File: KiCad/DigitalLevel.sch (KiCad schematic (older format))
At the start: 4 parts

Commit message: Adding KiCad PDF
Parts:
- removed U?: LD1117S33TR_SOT223, Package_TO_SOT_SMD:SOT-223-3_TabPin2, symbol Regulator_Linear:LD1117S33TR_SOT223
- added C1: 2200p, symbol Device:C
- added C2: 0.1u, symbol Device:C
- added C3: 0.01u, symbol Device:C
- added C4: 10n, symbol Device:C
- added R1, R2: 10k, symbol Device:R
- added U2: MPU-6050, Sensor_Motion:InvenSense_QFN-24_4x4mm_P0.5mm, symbol Sensor_Motion:MPU-6050
- added U3: XC6206P332MR, Package_TO_SOT_SMD:SOT-23, symbol Regulator_Linear:XC6206PxxxMR
- C5, C6: renamed from C?; value C -> 1u
- gave numbers to parts that had none: 1
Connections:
- net labels added: INT, SCL, SDA, VCC, VIN, VOUT, XCL, XDA
- wire segments 14 -> 55
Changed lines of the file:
@@
 $EndDescr
 $Comp
-L MCU_ST_STM32F1:STM32F103R6Tx U?
+L MCU_ST_STM32F1:STM32F103R6Tx U1
 U 1 1 5E2E5CE7
 P 3900 3550
-F 0 "U?" H 3900 1661 50  0000 C CNN
+F 0 "U1" H 3900 1661 50  0000 C CNN
 F 1 "STM32F103R6Tx" H 3900 1570 50  0000 C CNN
 F 2 "Package_QFP:LQFP-64_10x10mm_P0.5mm" H 3300 1850 50  0001 R CNN
 F 3 "http://www.st.com/st-web-ui/static/active/en/resource/technical/document/datasheet/CD00210843.pdf" H 3900 3550 50  0001 C CNN
 	1    3900 3550
-	1    0    0    -1
-$EndComp
-$Comp
-L Regulator_Linear:LD1117S33TR_SOT223 U?
-U 1 1 5E308040
-P 8200 2700
-F 0 "U?" H 8200 2942 50  0000 C CNN
-F 1 "LD1117S33TR_SOT223" H 8200 2851 50  0000 C CNN
-F 2 "Package_TO_SOT_SMD:SOT-223-3_TabPin2" H 8200 2900 50  0001 C CNN
-F 3 "http://www.st.com/st-web-ui/static/active/en/resource/technical/document/datasheet/CD00000544.pdf" H 8300 2450 50  0001 C CNN
-	1    8200 2700
 	1    0    0    -1
 $EndComp
@@
 Wire Wire Line
 	9900 5400 9900 5100
-Text GLabel 6100 5100 0    50   Input ~ 0
+Text GLabel 9300 5100 0    50   Input ~ 0
 GND
 Wire Wire Line
-	6100 5100 9900 5100
+	9300 5100 9900 5100
 Wire Wire Line
 	7900 2700 6950 2700
@@
 	9300 2700 9800 2700
 $Comp
-L Device:C C?
+L Device:C C6
 U 1 1 5E30AD7A
 P 9300 3200
-F 0 "C?" H 9415 3246 50  0000 L CNN
-F 1 "C" H 9415 3155 50  0000 L CNN
+F 0 "C6" H 9415 3246 50  0000 L CNN
+F 1 "1u" H 9415 3155 50  0000 L CNN
 F 2 "" H 9338 3050 50  0001 C CNN
 F 3 "~" H 9300 3200 50  0001 C CNN
@@
 $EndComp
 $Comp
-L Device:C C?
+L Device:C C5
 U 1 1 5E30B2D2
 P 6950 3200
-F 0 "C?" H 7065 3246 50  0000 L CNN
-F 1 "C" H 7065 3155 50  0000 L CNN
+F 0 "C5" H 7065 3246 50  0000 L CNN
+F 1 "1u" H 7065 3155 50  0000 L CNN
 F 2 "" H 6988 3050 50  0001 C CNN
 F 3 "~" H 6950 3200 50  0001 C CNN
@@
 Text GLabel 8200 3850 3    50   Input ~ 0
 GND
+$Comp
+L Regulator_Linear:XC6206PxxxMR U3
+U 1 1 5E2F309D
+P 8200 2700
+F 0 "U3" H 8200 2942 50  0000 C CNN
+F 1 "XC6206P332MR" H 8200 2851 50  0000 C CNN
+F 2 "Package_TO_SOT_SMD:SOT-23" H 8200 2925 50  0001 C CIN
+F 3 "https://www.torexsemi.com/file/xc6206/XC6206.pdf" H 8200 2700 50  0001 C CNN
+	1    8200 2700
+	1    0    0    -1
+$EndComp
+$Comp
+L Sensor_Motion:MPU-6050 U2
+U 1 1 5E2F4231
+P 2350 6550
+F 0 "U2" H 2350 5761 50  0000 C CNN
+F 1 "MPU-6050" H 2350 5670 50  0000 C CNN
+F 2 "Sensor_Motion:InvenSense_QFN-24_4x4mm_P0.5mm" H 2350 5750 50  0001 C CNN
+F 3 "https://store.invensense.com/datasheets/invensense/MPU-6050_DataSheet_V3%204.pdf" H 2350 6400 50  0001 C CNN
+	1    2350 6550
+	1    0    0    -1
+$EndComp
+Wire Wire Line
+	3050 6450 3350 6450
+Wire Wire Line
+	3050 6550 3350 6550
+Text GLabel 3350 6450 2    50   Input ~ 0
+XDA
+Text GLabel 3350 6550 2    50   Input ~ 0
+XCL
+Wire Wire Line
+	3050 6250 3350 6250
+Text GLabel 3350 6250 2    50   Input ~ 0
+INT
+Wire Wire Line
+	1650 6450 1250 6450
+Wire Wire Line
+	1250 6450 1250 7100
+$Comp
+L Device:R R2
+U 1 1 5E2F8CA7
+P 1250 7250
+F 0 "R2" H 1320 7296 50  0000 L CNN
+F 1 "10k" H 1320 7205 50  0000 L CNN
+F 2 "" V 1180 7250 50  0001 C CNN
+F 3 "~" H 1250 7250 50  0001 C CNN
+	1    1250 7250
+	1    0    0    -1
+$EndComp
+Wire Wire Line
+	1250 7400 1250 7600
+Wire Wire Line
+	1250 7600 1150 7600
+Text GLabel 950  7600 0    50   Input ~ 0
+GND
+Wire Wire Line
+	3050 6850 3350 6850
+Wire Wire Line
+	3350 6850 3350 7100
+$Comp
+L Device:C C2
+U 1 1 5E2FCE8B
+P 3350 7250
+F 0 "C2" H 3465 7296 50  0000 L CNN
+F 1 "0.1u" H 3465 7205 50  0000 L CNN
+F 2 "" H 3388 7100 50  0001 C CNN
+F 3 "~" H 3350 7250 50  0001 C CNN
+	1    3350 7250
+	1    0    0    -1
+$EndComp
+Wire Wire Line
+	3350 7400 3350 7600
+Wire Wire Line
+	3350 7600 2350 7600
+Connection ~ 1250 7600
+Wire Wire Line
+	1650 6750 1550 6750
+Wire Wire Line
+	1550 6750 1550 7100
+$Comp
+L Device:R R1
+U 1 1 5E2FE974
+P 1550 7250
+F 0 "R1" H 1620 7296 50  0000 L CNN
+F 1 "10k" H 1620 7205 50  0000 L CNN
+F 2 "" V 1480 7250 50  0001 C CNN
+F 3 "~" H 1550 7250 50  0001 C CNN
+	1    1550 7250
+	1    0    0    -1
+$EndComp
+Wire Wire Line
+	1550 7400 1550 7600
+Connection ~ 1550 7600
+Wire Wire Line
+	1550 7600 1250 7600
+$Comp
+L Device:C C1
+U 1 1 5E305EAE
+P 3800 7250
+F 0 "C1" H 3915 7296 50  0000 L CNN
+F 1 "2200p" H 3915 7205 50  0000 L CNN
+F 2 "" H 3838 7100 50  0001 C CNN
+F 3 "~" H 3800 7250 50  0001 C CNN
+	1    3800 7250
+	1    0    0    -1
+$EndComp
+Wire Wire Line
+	3050 6750 3800 6750
+Wire Wire Line
+	3800 6750 3800 7100
+Connection ~ 3350 7600
+Wire Wire Line
+	2450 5850 2450 5750
+Text GLabel 2450 5650 1    50   Input ~ 0
+VCC
+Text GLabel 1150 6250 0    50   Input ~ 0
+SDA
+Text GLabel 1150 6350 0    50   Input ~ 0
+SCL
+Wire Wire Line
+	1150 6350 1650 6350
+Wire Wire Line
+	1150 6250 1650 6250
+Wire Wire Line
+	3800 7400 3800 7600
+Wire Wire Line
+	3350 7600 3800 7600
+Wire Wire Line
+	2250 5850 2250 5750
+Wire Wire Line
+	1150 6850 1150 7600
+Wire Wire Line
+	1150 6850 1650 6850
+Connection ~ 1150 7600
+Wire Wire Line
+	1150 7600 950  7600
+Wire Wire Line
+	1150 6850 800  6850
+Wire Wire Line
+	800  6850 800  6950
+Connection ~ 1150 6850
+$Comp
+L Device:C C3
+U 1 1 5E31CE3D
+P 800 7100
+F 0 "C3" H 915 7146 50  0000 L CNN
+F 1 "0.01u" H 915 7055 50  0000 L CNN
+F 2 "" H 838 6950 50  0001 C CNN
+F 3 "~" H 800 7100 50  0001 C CNN
+	1    800  7100
+	1    0    0    -1
+$EndComp
+Wire Wire Line
+	800  7250 800  7300
+Text GLabel 800  7300 3    50   Input ~ 0
+VCC
+Wire Wire Line
+	2250 5750 1800 5750
+Wire Wire Line
+	1800 5750 1800 5650
+Connection ~ 2250 5750
+$Comp
+L Device:C C4
+U 1 1 5E3215BB
+P 1800 5500
+F 0 "C4" H 1915 5546 50  0000 L CNN
+F 1 "10n" H 1915 5455 50  0000 L CNN
+F 2 "" H 1838 5350 50  0001 C CNN
+F 3 "~" H 1800 5500 50  0001 C CNN
+	1    1800 5500
+	1    0    0    -1
+$EndComp
+Wire Wire Line
+	1800 5350 1800 5300
+Wire Wire Line
+	1800 5300 3000 5300
+Wire Wire Line
+	3000 5300 3000 5900
+Wire Wire Line
+	3000 5900 4250 5900
+Wire Wire Line
+	4250 5900 4250 7600
+Wire Wire Line
+	4250 7600 3800 7600
+Connection ~ 3800 7600
+Wire Wire Line
+	2250 5750 2450 5750
+Connection ~ 2450 5750
+Wire Wire Line
+	2450 5750 2450 5650
+Wire Wire Line
+	2350 7250 2350 7600
+Connection ~ 2350 7600
+Wire Wire Line
+	2350 7600 1550 7600
+Text GLabel 6400 2700 0    50   Input ~ 0
+VIN
+Text GLabel 9800 2700 2    50   Input ~ 0
+VOUT
 $EndSCHEMATC

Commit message: Updated Block Diagram and Schematics
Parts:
- added D? (x25): LED, symbol Device:LED
- added R10, R11, R12, R13, R14, R15, R16, R17, R18, R19, R20, R21, R22, R23, R24, R25, R26, R27, R3, R4, R5, R6, R7, R8, R9: 1k, symbol Device:R
- added R28: 3.3k, symbol Device:R
- added SW1, SW2, SW3: SW_Push_Open, symbol Switch:SW_Push_Open
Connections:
- net labels added: BTN1, BTN2, BTN3, DIODE-SW, DIODE1, DIODE2
- wire segments 55 -> 141

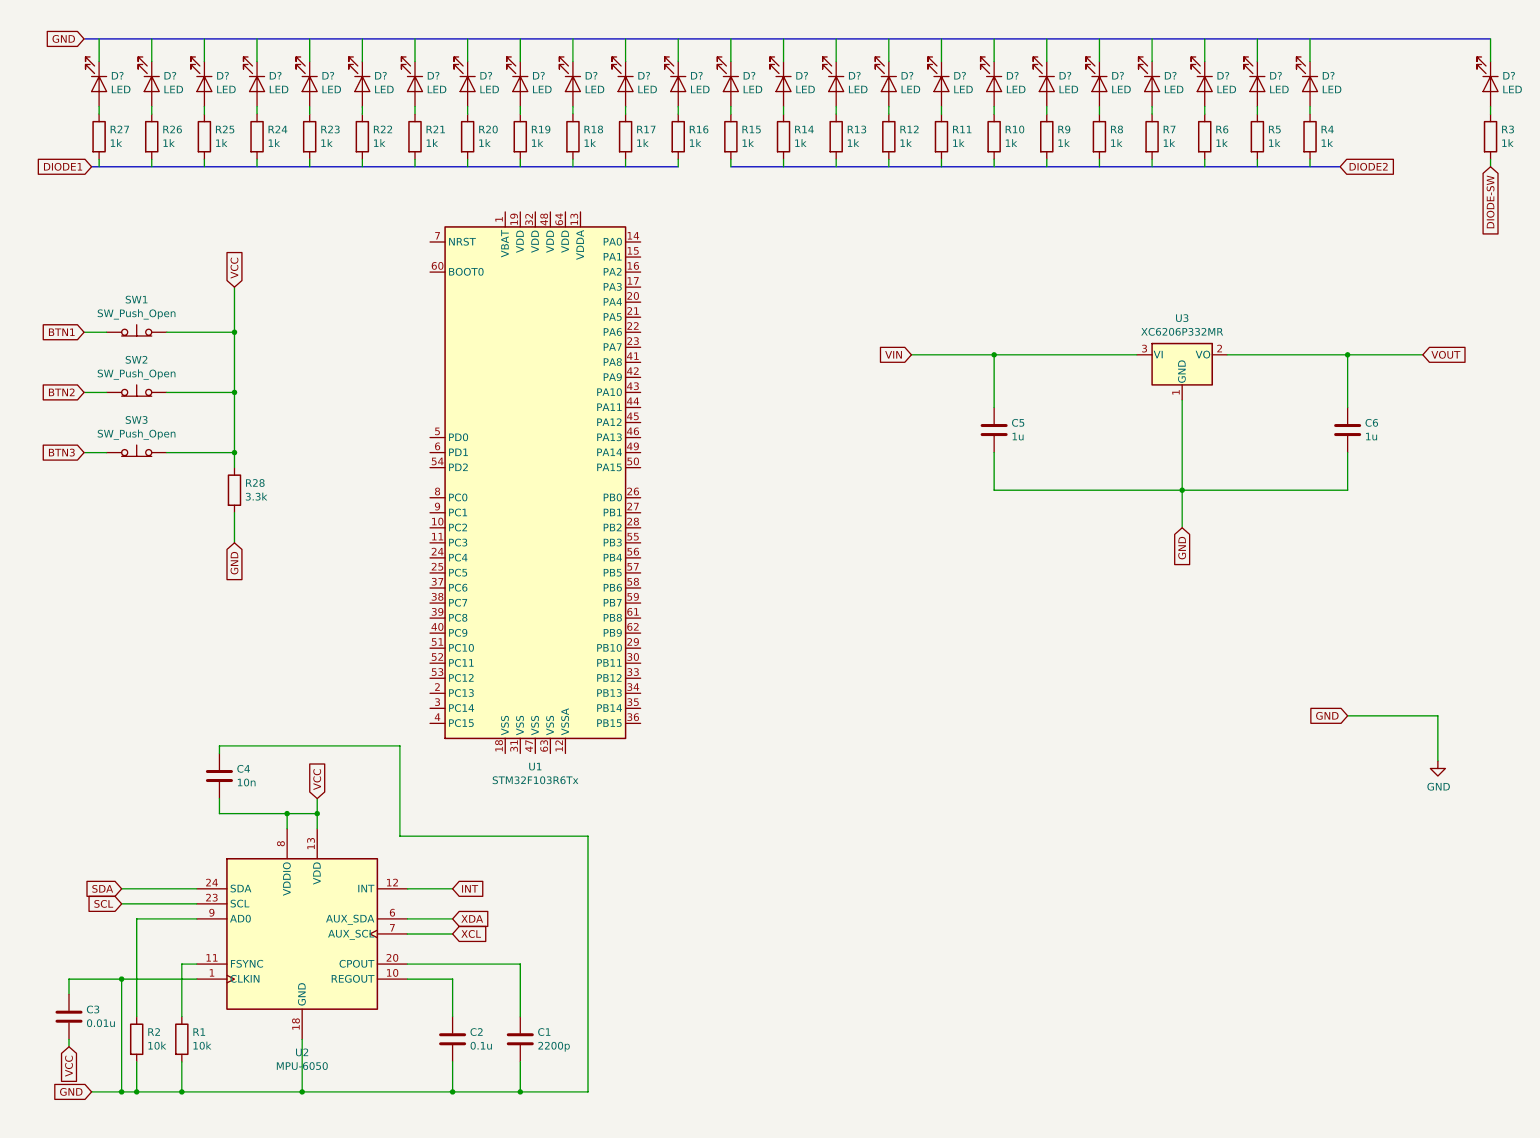
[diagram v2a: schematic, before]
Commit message: Fixed schematics
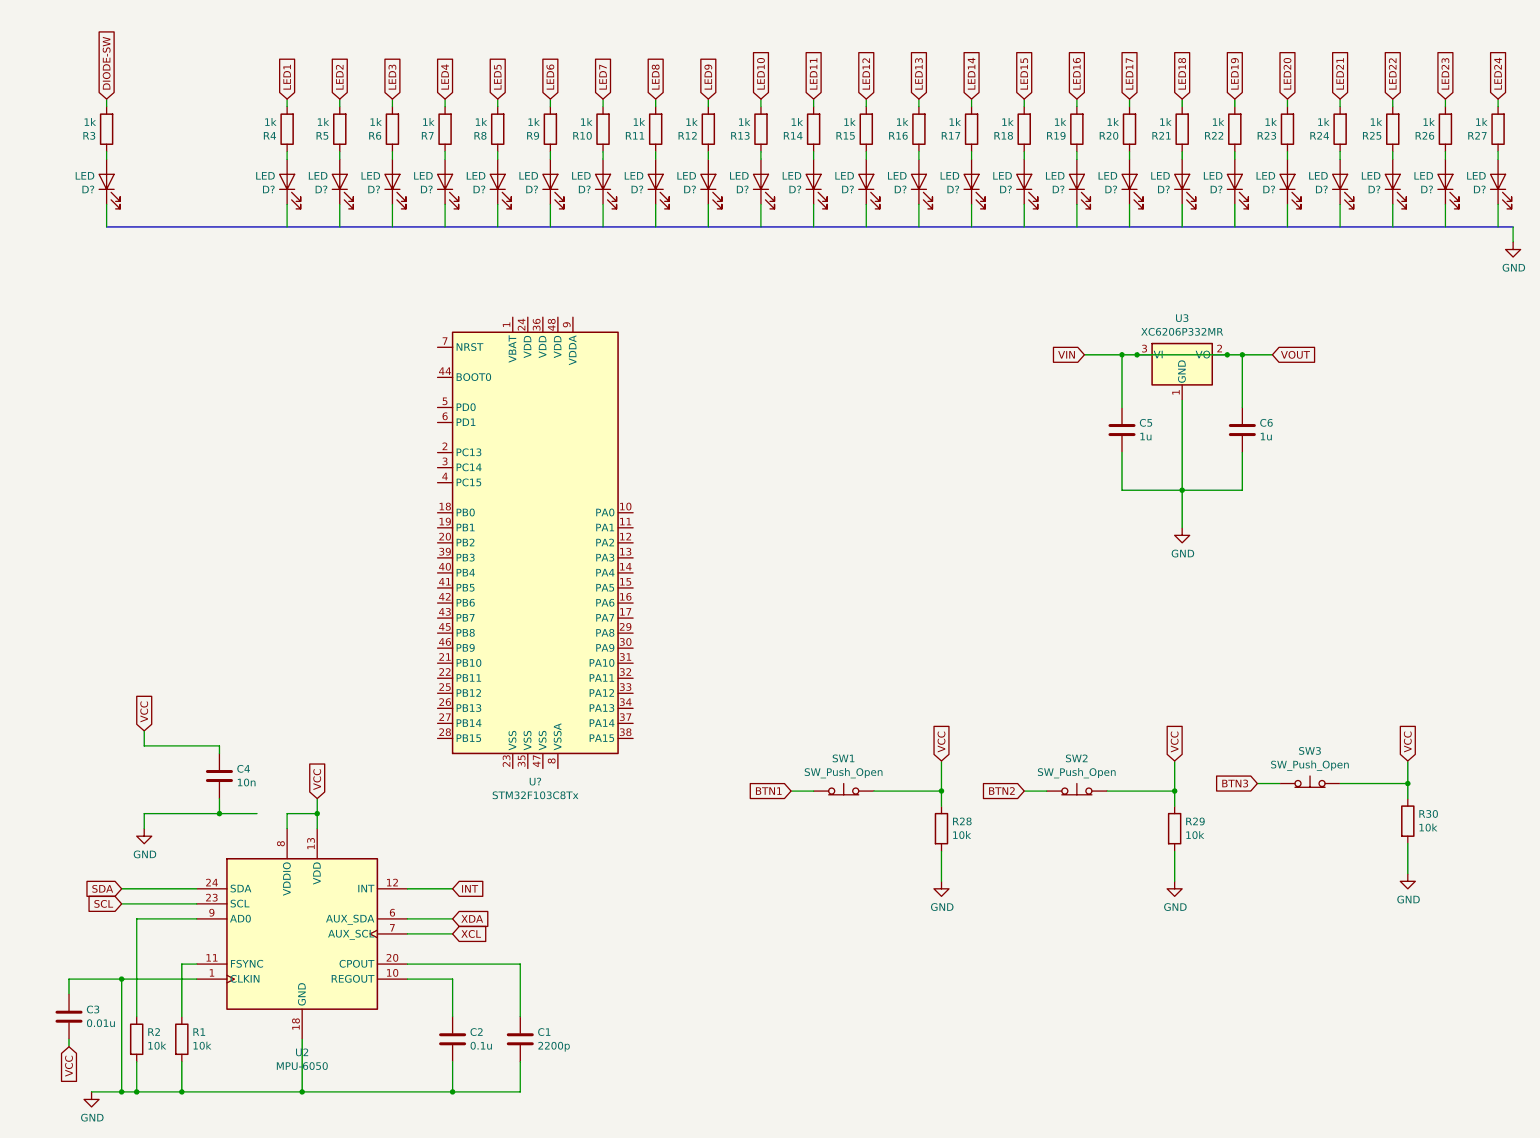
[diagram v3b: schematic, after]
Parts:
- removed SW2: SW_Push_Open, symbol Switch:SW_Push_Open
- removed U1: STM32F103R6Tx, Package_QFP:LQFP-64_10x10mm_P0.5mm, symbol MCU_ST_STM32F1:STM32F103R6Tx
- added R28, R30: 10k, symbol Device:R
- added SW3: SW_Push_Open, symbol Switch:SW_Push_Open
- added U?: STM32F103C8Tx, Package_QFP:LQFP-48_7x7mm_P0.5mm, symbol MCU_ST_STM32F1:STM32F103C8Tx
- R29: renamed from R28; value 3.3k -> 10k
- renumbered SW3 to SW2
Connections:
- net labels added: LED1, LED10, LED11, LED12, LED13, LED14, LED15, LED16, LED17, LED18, LED19, LED2, LED20, LED21, LED22, LED23, LED24, LED3, LED4, LED5, LED6, LED7, LED8, LED9
- net labels removed: DIODE1, DIODE2
- wire segments 141 -> 144
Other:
- moved on the sheet: C5, C6, D?, R10, R11, R12, R13, R14, R15, R16, R17, R18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

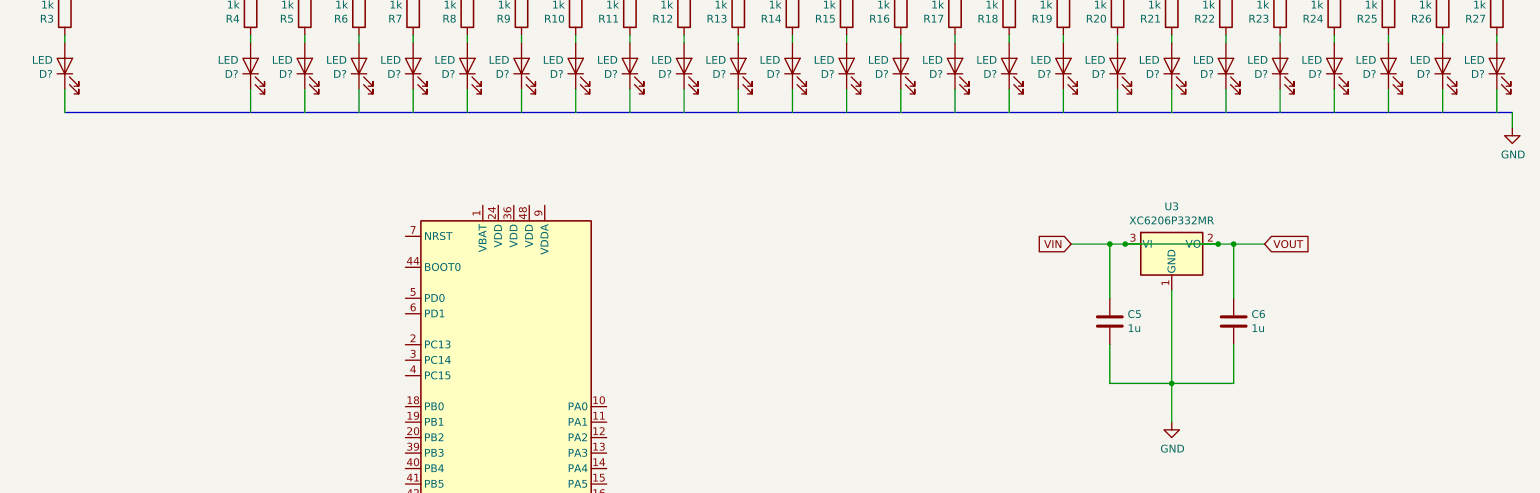
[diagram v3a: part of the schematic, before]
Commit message: Fixed schematics
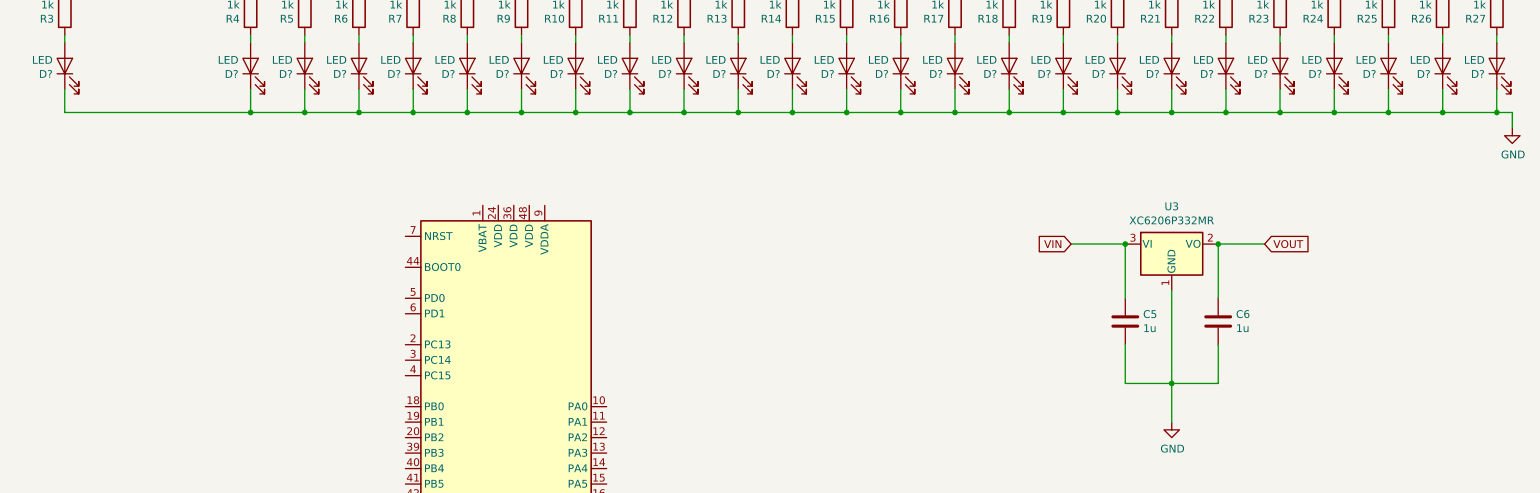
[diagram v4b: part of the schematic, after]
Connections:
- wire segments 144 -> 166
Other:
- moved on the sheet: C5, C6
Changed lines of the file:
@@
 $EndDescr
 Wire Wire Line
-	7900 2700 7800 2700
-Wire Wire Line
-	7800 2700 7800 3050
-Wire Wire Line
-	8600 2700 8600 3050
+	7900 2700 7900 3050
+Wire Wire Line
+	8500 2700 8500 3050
 $Comp
 L Device:C C6
 U 1 1 5E30AD7A
-P 8600 3200
-F 0 "C6" H 8715 3246 50  0000 L CNN
-F 1 "1u" H 8715 3155 50  0000 L CNN
-F 2 "" H 8638 3050 50  0001 C CNN
-F 3 "~" H 8600 3200 50  0001 C CNN
-	1    8600 3200
-	1    0    0    -1
-$EndComp
-$Comp
-L Device:C C5
-U 1 1 5E30B2D2
-P 7800 3200
-F 0 "C5" H 7915 3246 50  0000 L CNN
-F 1 "1u" H 7915 3155 50  0000 L CNN
-F 2 "" H 7838 3050 50  0001 C CNN
-F 3 "~" H 7800 3200 50  0001 C CNN
-	1    7800 3200
-	1    0    0    -1
-$EndComp
-Wire Wire Line
-	7800 3350 7800 3600
-Wire Wire Line
-	8600 3600 8600 3350
+P 8500 3200
+F 0 "C6" H 8615 3246 50  0000 L CNN
+F 1 "1u" H 8615 3155 50  0000 L CNN
+F 2 "" H 8538 3050 50  0001 C CNN
+F 3 "~" H 8500 3200 50  0001 C CNN
+	1    8500 3200
+	1    0    0    -1
+$EndComp
+Wire Wire Line
+	8500 3600 8500 3350
 Wire Wire Line
 	8200 3000 8200 3600
 Connection ~ 8200 3600
 Wire Wire Line
-	8200 3600 8600 3600
+	8200 3600 8500 3600
 Wire Wire Line
 	8200 3600 8200 3850
@@
 Text GLabel 1050 1000 1    50   Input ~ 0
 DIODE-SW
-Wire Bus Line
-	10400 1850 1050 1850
 Wire Wire Line
 	10300 1700 10300 1850
@@
 Wire Wire Line
 	10400 1950 10400 1850
-Wire Wire Line
-	7800 3600 8200 3600
-Connection ~ 7900 2700
-Wire Wire Line
-	7900 2700 8500 2700
-Wire Wire Line
-	8600 2700 8800 2700
-Wire Wire Line
-	7550 2700 7800 2700
-Connection ~ 7800 2700
-Wire Wire Line
-	8500 2700 8600 2700
-Connection ~ 8500 2700
-Connection ~ 8600 2700
 $Comp
 L power:GND #PWR?
@@
 Text GLabel 1300 5200 1    50   Input ~ 0
 VCC
+Wire Wire Line
+	8500 2700 8800 2700
+Wire Wire Line
+	7900 3350 7900 3600
+$Comp
+L Device:C C5
+U 1 1 5E30B2D2
+P 7900 3200
+F 0 "C5" H 8015 3246 50  0000 L CNN
+F 1 "1u" H 8015 3155 50  0000 L CNN
+F 2 "" H 7938 3050 50  0001 C CNN
+F 3 "~" H 7900 3200 50  0001 C CNN
+	1    7900 3200
+	1    0    0    -1
+$EndComp
+Wire Wire Line
+	7900 3600 8200 3600
+Wire Wire Line
+	7550 2700 7900 2700
+Connection ~ 7900 2700
+Connection ~ 8500 2700
+Wire Wire Line
+	10400 1850 10300 1850
+Wire Wire Line
+	10300 1850 9950 1850
+Connection ~ 10300 1850
+Connection ~ 2600 1850
+Wire Wire Line
+	2600 1850 2250 1850
+Connection ~ 2950 1850
+Wire Wire Line
+	2950 1850 2600 1850
+Connection ~ 3300 1850
+Wire Wire Line
+	3300 1850 2950 1850
+Connection ~ 3650 1850
+Wire Wire Line
+	3650 1850 3300 1850
+Connection ~ 4000 1850
+Wire Wire Line
+	4000 1850 3650 1850
+Connection ~ 4350 1850
+Wire Wire Line
+	4350 1850 4000 1850
+Connection ~ 4700 1850
+Wire Wire Line
+	4700 1850 4350 1850
+Connection ~ 5050 1850
+Wire Wire Line
+	5050 1850 4700 1850
+Connection ~ 5400 1850
+Wire Wire Line
+	5400 1850 5050 1850
+Connection ~ 5750 1850
+Wire Wire Line
+	5750 1850 5400 1850
+Connection ~ 6100 1850
+Wire Wire Line
+	6100 1850 5750 1850
+Connection ~ 6450 1850
+Wire Wire Line
+	6450 1850 6100 1850
+Connection ~ 6800 1850
+Wire Wire Line
+	6800 1850 6450 1850
+Connection ~ 7150 1850
+Wire Wire Line
+	7150 1850 6800 1850
+Connection ~ 7500 1850
+Wire Wire Line
+	7500 1850 7150 1850
+Connection ~ 7850 1850
+Wire Wire Line
+	7850 1850 7500 1850
+Connection ~ 8200 1850
+Wire Wire Line
+	8200 1850 7850 1850
+Connection ~ 8550 1850
+Wire Wire Line
+	8550 1850 8200 1850
+Connection ~ 8900 1850
+Wire Wire Line
+	8900 1850 8550 1850
+Connection ~ 9250 1850
+Wire Wire Line
+	9250 1850 8900 1850
+Connection ~ 9600 1850
+Wire Wire Line
+	9600 1850 9250 1850
+Connection ~ 9950 1850
+Wire Wire Line
+	9950 1850 9600 1850
+Wire Wire Line
+	1050 1850 2250 1850
+Connection ~ 2250 1850
 $EndSCHEMATC
